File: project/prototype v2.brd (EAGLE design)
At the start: 70.5 x 38.1 mm, 50 parts, among them M1 NX7002AK, M10 NX7002AK, M12 NX7002AK, M3 NX7002AK, M4 NX7002AK, M5 NX7002AK, M6 NX7002AK, M8 NX7002AK, X1 RJ12, X2 RJ12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

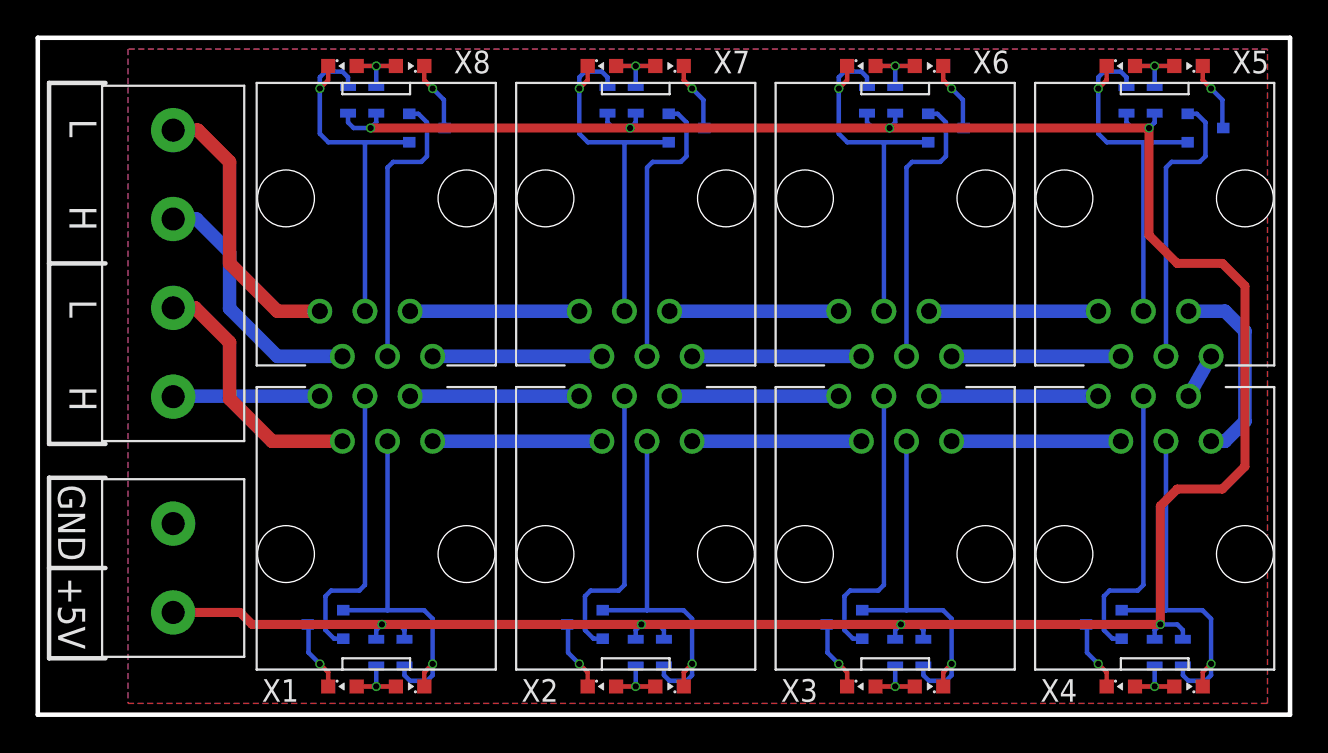
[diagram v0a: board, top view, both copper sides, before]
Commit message: Update RJ12 position
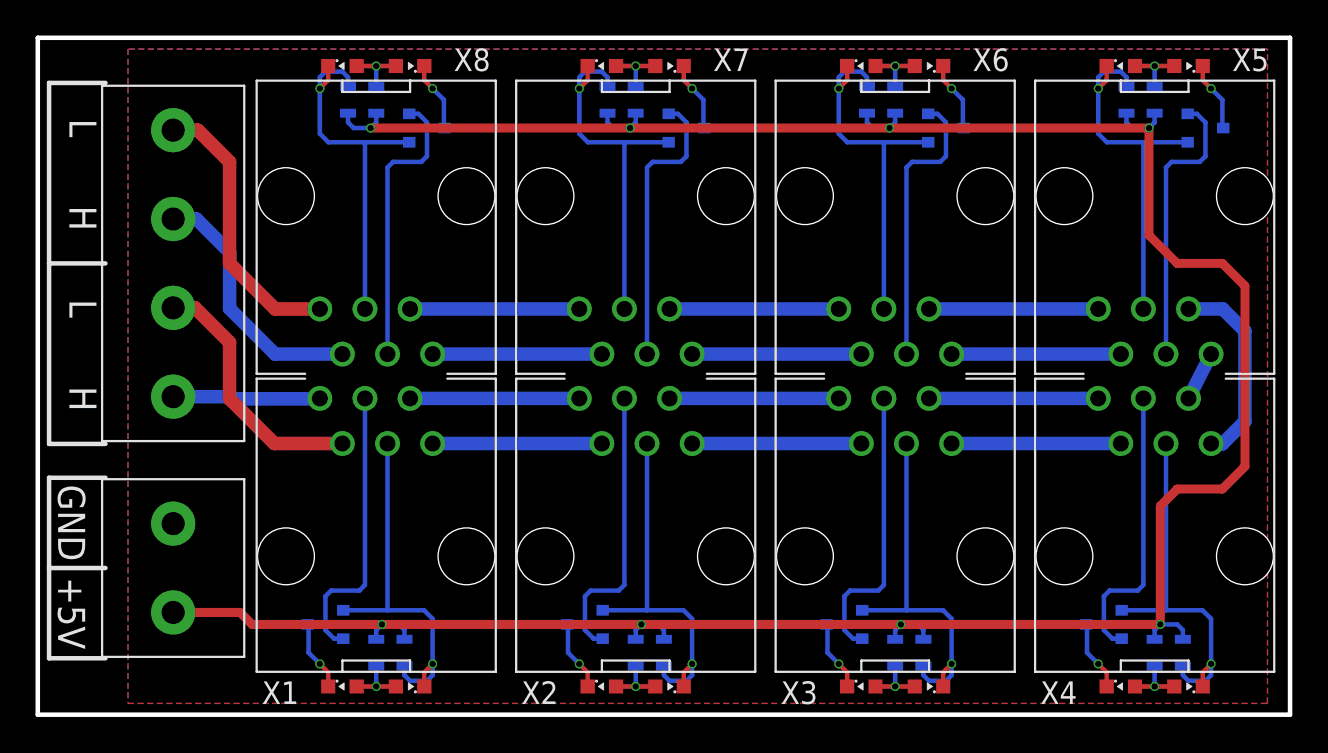
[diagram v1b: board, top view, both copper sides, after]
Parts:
- moved X1 0.13 mm to (19.1, 2.41)
- moved X2 0.13 mm to (33.7, 2.41)
- moved X3 0.13 mm to (48.3, 2.41)
- moved X4 0.13 mm to (62.9, 2.41)
- moved X5 0.13 mm to (62.9, 35.7)
- moved X6 0.13 mm to (48.3, 35.7)
- moved X7 0.13 mm to (33.7, 35.7)
- moved X8 0.13 mm to (19.1, 35.7)
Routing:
- net GND: track 129.7 -> 128.7 mm
